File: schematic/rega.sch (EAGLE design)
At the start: 42 parts, among them IC1 ESP8266_ESP-12, K1 FRS1B, K2 351, K3 351, Q100 BSS123, Q101 2N7002, Q102 2N7002, X1 GMSTBA2, X2 GMSTBA2

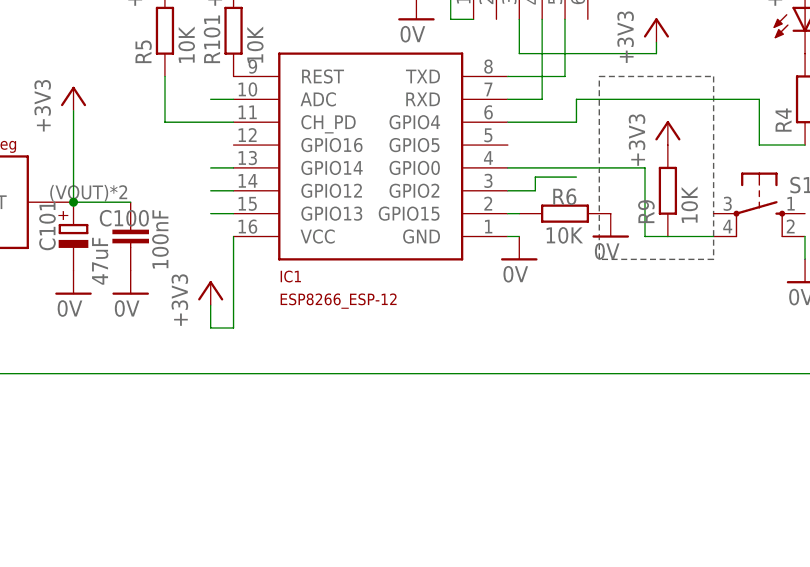
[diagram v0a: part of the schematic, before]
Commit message: HW add missing resistor GPIO2 High
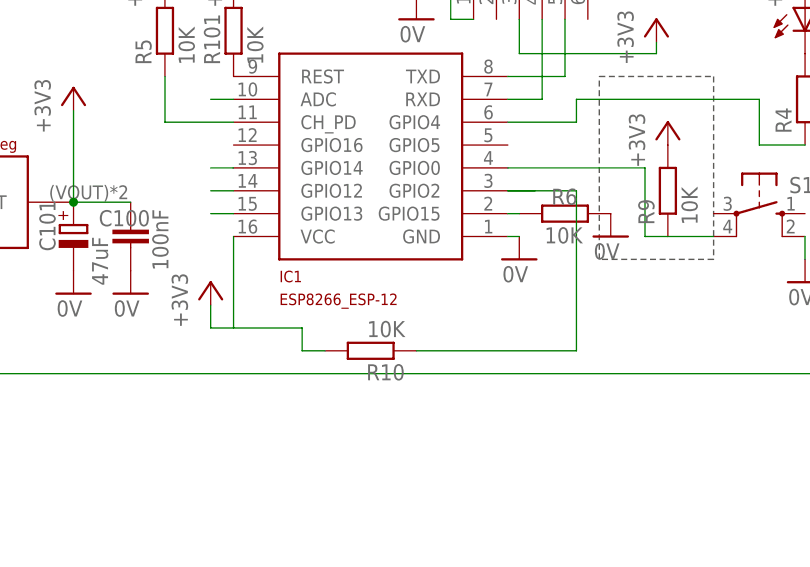
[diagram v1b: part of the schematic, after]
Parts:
- added R10: 10K, rcl:R-EU_R0805
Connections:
- net +3V3: now also R10.2
- net GPIO2: now also R10.1
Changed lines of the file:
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@@
 <part name="R9" library="rcl" deviceset="R-EU_" device="R0805" value="10K"/>
 <part name="+3V8" library="supply1" deviceset="+3V3" device=""/>
+<part name="R10" library="rcl" deviceset="R-EU_" device="R0805" value="10K"/>
 </parts>
 <sheets>
@@
 <instance part="R9" gate="G$1" x="114.3" y="71.12" rot="R90"/>
 <instance part="+3V8" gate="G$1" x="114.3" y="78.74"/>
+<instance part="R10" gate="G$1" x="81.28" y="53.34" rot="R180"/>
 </instances>
 <busses>
@@
 <wire x1="66.04" y1="55.88" x2="66.04" y2="66.04" width="0.1524" layer="91"/>
 <pinref part="+3V2" gate="G$1" pin="+3V3"/>
+<wire x1="66.04" y1="55.88" x2="73.66" y2="55.88" width="0.1524" layer="91"/>
+<wire x1="73.66" y1="55.88" x2="73.66" y2="53.34" width="0.1524" layer="91"/>
+<pinref part="R10" gate="G$1" pin="2"/>
+<wire x1="73.66" y1="53.34" x2="76.2" y2="53.34" width="0.1524" layer="91"/>
 </segment>
 <segment>
@@
 <segment>
 <wire x1="96.52" y1="71.12" x2="99.568" y2="71.12" width="0.1524" layer="91"/>
-<wire x1="99.568" y1="71.12" x2="99.568" y2="72.644" width="0.1524" layer="91"/>
-<wire x1="99.568" y1="72.644" x2="104.14" y2="72.644" width="0.1524" layer="91"/>
 <pinref part="IC1" gate="G$1" pin="GPIO2"/>
-</segment>
-</net>
+<wire x1="96.52" y1="71.12" x2="104.14" y2="71.12" width="0.1524" layer="91"/>
+<wire x1="104.14" y1="71.12" x2="104.14" y2="53.34" width="0.1524" layer="91"/>
+<pinref part="R10" gate="G$1" pin="1"/>
+<wire x1="104.14" y1="53.34" x2="86.36" y2="53.34" width="0.1524" layer="91"/>
+</segment>
+</net>
